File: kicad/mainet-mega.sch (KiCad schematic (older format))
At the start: 30 parts, among them J1 Screw_Terminal_01x03, J10 Screw_Terminal_01x03, J11 Screw_Terminal_01x03, J12 Screw_Terminal_01x03, J13 Screw_Terminal_01x03, J14 Screw_Terminal_01x03, J15 Screw_Terminal_01x03, J16 Screw_Terminal_01x03, J17 Screw_Terminal_01x03, J18 Screw_Terminal_01x03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

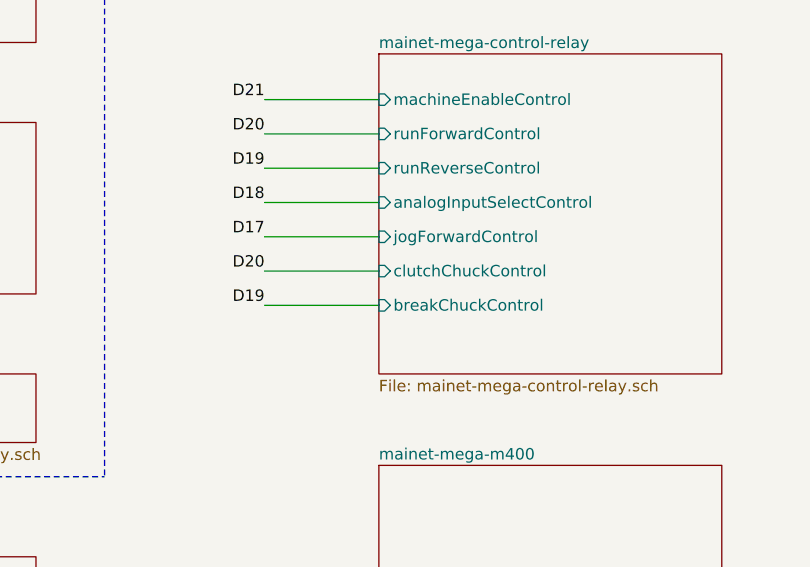
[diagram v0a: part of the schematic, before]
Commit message: KICAD: Cambio etiqueta breakChuck a brakeChuck y correción del pin
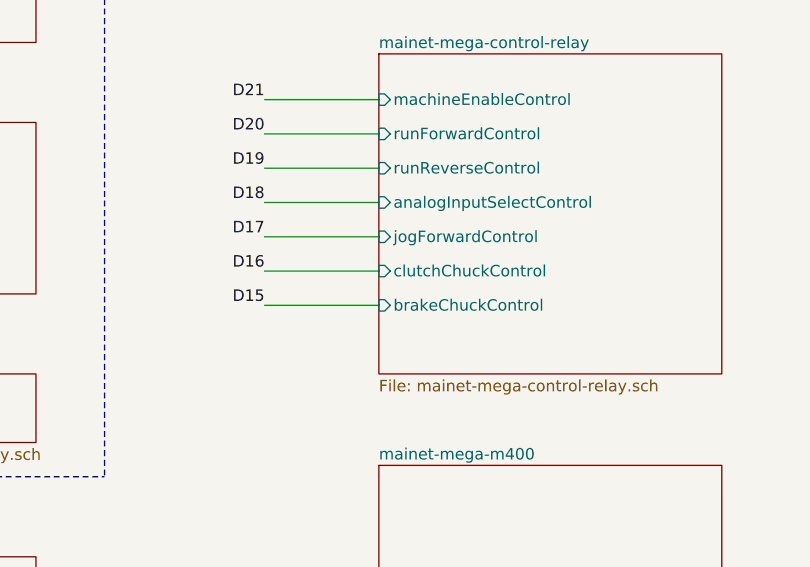
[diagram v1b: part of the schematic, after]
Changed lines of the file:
@@
 F6 "jogForwardControl" I L 9100 2900 50
 F7 "clutchChuckControl" I L 9100 3050 50
-F8 "breakChuckControl" I L 9100 3200 50
+F8 "brakeChuckControl" I L 9100 3200 50
 $EndSheet
 Wire Wire Line
@@
 	9100 3200 8600 3200
 Text Label 8600 3050 2    50   ~ 0
-D20
+D16
 Text Label 8600 3200 2    50   ~ 0
-D19
+D15
 Wire Wire Line
 	5650 1050 6100 1050

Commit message: KICAD: Actualizar sch Fecha y versión
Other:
- note removed: "27/01/2021"
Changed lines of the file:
@@
 encoding utf-8
 Sheet 1 21
-Title ""
-Date ""
-Rev ""
+Title "Mainet-mega -- "
+Date "2021-03-24"
+Rev "1.0"
 Comp ""
 Comment1 ""
@@
 F1 "mainet-mega-emergencyStopRelay.sch" 50
 $EndSheet
-Text Notes 10600 7650 0    50   ~ 0
-27/01/2021
 $Sheet
 S 6100 900  1500 1150
